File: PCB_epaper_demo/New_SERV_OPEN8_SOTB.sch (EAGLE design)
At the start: 71 parts, among them IC2 LT3082EST#PBF, IC3 RP105x, IC4 SN74AUP1G00DCKR, IC5 SN74AUP1G00DCKR, IC6 LM358AMX_NOPB, J1 TB006-508-02BE, J2 TB006-508-02BE, U1 SN74LVC1G32DBVR, U3 SN74AUP1G14DBVR, Y1 KC7050A48.0000C50D00

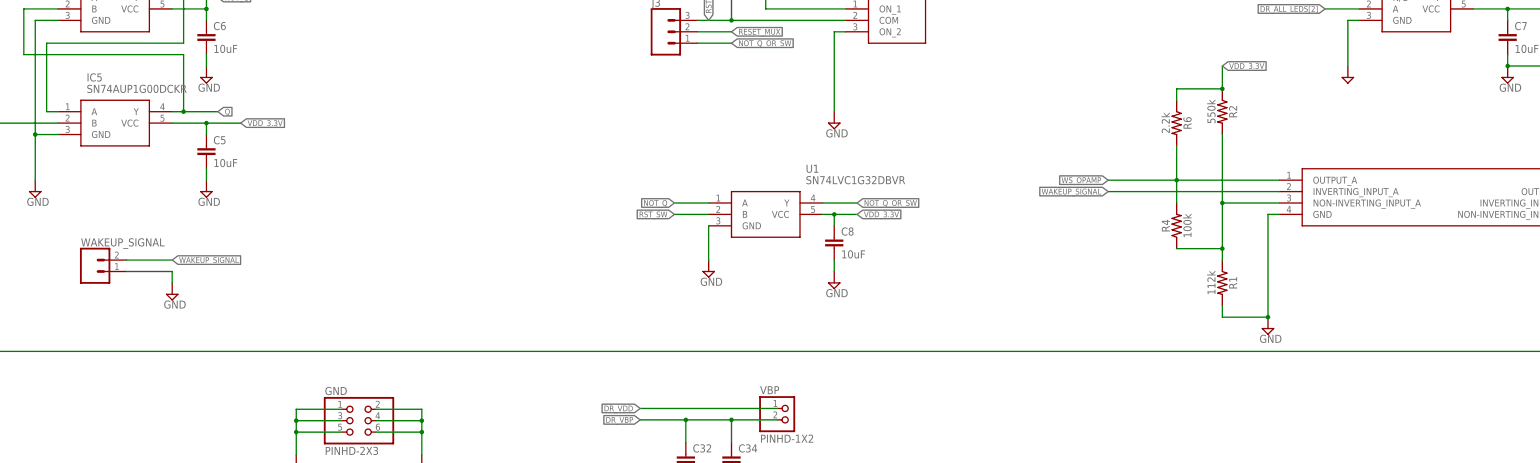
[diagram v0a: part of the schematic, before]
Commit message: add trimmer
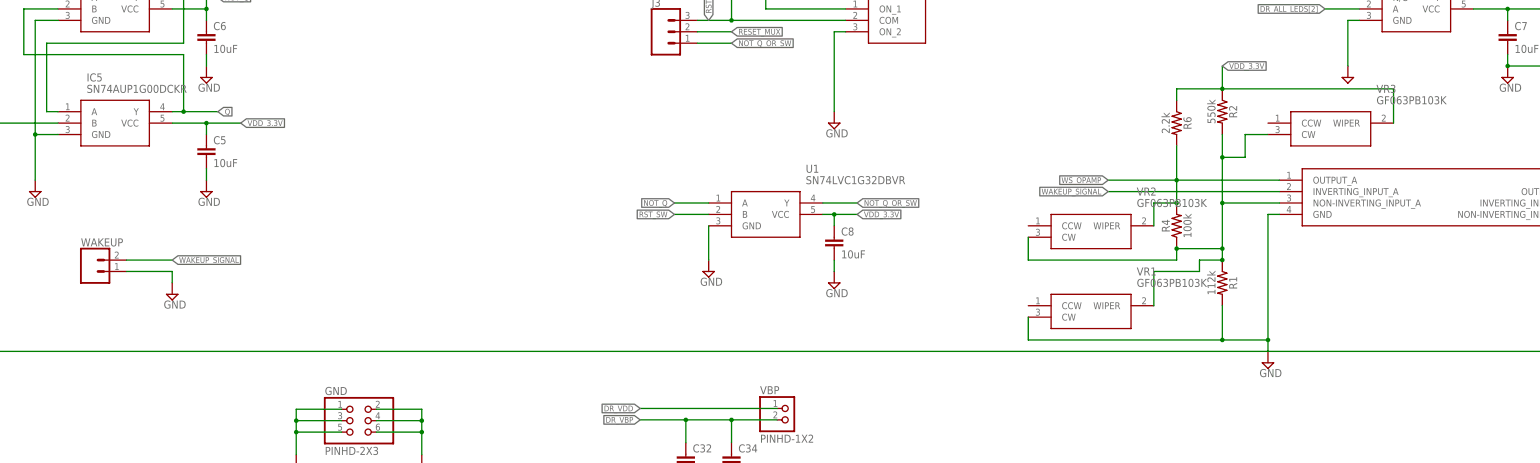
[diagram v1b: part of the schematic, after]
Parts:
- added VR1, VR2, VR3: GF063PB103K, SamacSys_Parts:GF063PB103K
- renumbered WAKEUP_SIGNAL to WAKEUP
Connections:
- net GND: now also VR1.CW
- net N$4: now also VR1.WIPER, VR2.CW, VR3.CW
- net VDD_3.3V: now also VR3.WIPER
- net WS_OPAMP: now also VR2.WIPER
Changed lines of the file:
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@@
 <part name="SUPPLY20" library="supply2" library_urn="urn:adsk.eagle:library:372" deviceset="GND" device=""/>
 <part name="LED" library="SparkFun-Connectors" library_urn="urn:adsk.eagle:library:513" deviceset="CONN_01" device="" package3d_urn="urn:adsk.eagle:package:38028/1"/>
-<part name="WAKEUP_SIGNAL" library="SparkFun-Connectors" library_urn="urn:adsk.eagle:library:513" deviceset="CONN_02" device="" package3d_urn="urn:adsk.eagle:package:38039/1"/>
+<part name="WAKEUP" library="SparkFun-Connectors" library_urn="urn:adsk.eagle:library:513" deviceset="CONN_02" device="" package3d_urn="urn:adsk.eagle:package:38039/1"/>
 <part name="SUPPLY21" library="supply2" library_urn="urn:adsk.eagle:library:372" deviceset="GND" device=""/>
 <part name="C9" library="SparkFun-Capacitors" library_urn="urn:adsk.eagle:library:510" deviceset="1.0UF" device="-0805-25V-(+80/-20%)" package3d_urn="urn:adsk.eagle:package:37429/1" value="0.1uF"/>
@@
 <part name="0.9V" library="Connector" library_urn="urn:adsk.eagle:library:16378166" deviceset="PINHD-1X3" device="" package3d_urn="urn:adsk.eagle:package:22458/2"/>
 <part name="R7" library="SparkFun-Resistors" library_urn="urn:adsk.eagle:library:532" deviceset="0.3OHM" device="-0805-1/8W-1%" package3d_urn="urn:adsk.eagle:package:39651/1" value="10k"/>
+<part name="VR1" library="SamacSys_Parts" deviceset="GF063PB103K" device=""/>
+<part name="VR2" library="SamacSys_Parts" deviceset="GF063PB103K" device=""/>
+<part name="VR3" library="SamacSys_Parts" deviceset="GF063PB103K" device=""/>
 </parts>
 <sheets>
@@
 <attribute name="NAME" x="154.94" y="106.172" size="1.778" layer="95" font="vector" rot="R180"/>
 </instance>
-<instance part="WAKEUP_SIGNAL" gate="G$1" x="-66.04" y="-76.2" smashed="yes">
+<instance part="WAKEUP" gate="G$1" x="-66.04" y="-76.2" smashed="yes">
 <attribute name="VALUE" x="-68.58" y="-81.026" size="1.778" layer="96" font="vector"/>
 <attribute name="NAME" x="-68.58" y="-70.612" size="1.778" layer="95" font="vector"/>
@@
 <attribute name="VALUE" x="265.43" y="-50.8" size="1.778" layer="96" align="center-left"/>
 </instance>
-<instance part="SUPPLY5" gate="GND" x="195.58" y="-88.9" smashed="yes">
-<attribute name="VALUE" x="193.675" y="-92.075" size="1.778" layer="96"/>
+<instance part="SUPPLY5" gate="GND" x="195.58" y="-96.52" smashed="yes">
+<attribute name="VALUE" x="193.675" y="-99.695" size="1.778" layer="96"/>
 </instance>
 <instance part="R1" gate="G$1" x="185.42" y="-78.74" smashed="yes" rot="R270">
@@
 <attribute name="NAME" x="77.724" y="-10.16" size="1.778" layer="95" font="vector" rot="R270" align="bottom-center"/>
 <attribute name="VALUE" x="74.676" y="-10.16" size="1.778" layer="96" font="vector" rot="R270" align="top-center"/>
+</instance>
+<instance part="VR1" gate="G$1" x="142.24" y="-83.82" smashed="yes">
+<attribute name="NAME" x="166.37" y="-76.2" size="1.778" layer="95" align="center-left"/>
+<attribute name="VALUE" x="166.37" y="-78.74" size="1.778" layer="96" align="center-left"/>
+</instance>
+<instance part="VR2" gate="G$1" x="142.24" y="-66.04" smashed="yes">
+<attribute name="NAME" x="166.37" y="-58.42" size="1.778" layer="95" align="center-left"/>
+<attribute name="VALUE" x="166.37" y="-60.96" size="1.778" layer="96" align="center-left"/>
+</instance>
+<instance part="VR3" gate="G$1" x="195.58" y="-43.18" smashed="yes">
+<attribute name="NAME" x="219.71" y="-35.56" size="1.778" layer="95" align="center-left"/>
+<attribute name="VALUE" x="219.71" y="-38.1" size="1.778" layer="96" align="center-left"/>
 </instance>
 </instances>
@@
 </segment>
 <segment>
-<pinref part="WAKEUP_SIGNAL" gate="G$1" pin="1"/>
+<pinref part="WAKEUP" gate="G$1" pin="1"/>
 <wire x1="-58.42" y1="-76.2" x2="-48.26" y2="-76.2" width="0.1524" layer="91"/>
 <pinref part="SUPPLY21" gate="GND" pin="GND"/>
@@
 <pinref part="IC6" gate="G$1" pin="GND"/>
 <wire x1="198.12" y1="-63.5" x2="195.58" y2="-63.5" width="0.1524" layer="91"/>
-<wire x1="195.58" y1="-63.5" x2="195.58" y2="-86.36" width="0.1524" layer="91"/>
+<wire x1="195.58" y1="-63.5" x2="195.58" y2="-91.44" width="0.1524" layer="91"/>
 <pinref part="SUPPLY5" gate="GND" pin="GND"/>
+<pinref part="VR1" gate="G$1" pin="CW"/>
+<wire x1="195.58" y1="-91.44" x2="195.58" y2="-93.98" width="0.1524" layer="91"/>
+<wire x1="142.24" y1="-86.36" x2="142.24" y2="-91.44" width="0.1524" layer="91"/>
 <pinref part="R1" gate="G$1" pin="2"/>
-<wire x1="185.42" y1="-83.82" x2="185.42" y2="-86.36" width="0.1524" layer="91"/>
-<wire x1="185.42" y1="-86.36" x2="195.58" y2="-86.36" width="0.1524" layer="91"/>
-<junction x="195.58" y="-86.36"/>
+<wire x1="142.24" y1="-91.44" x2="185.42" y2="-91.44" width="0.1524" layer="91"/>
+<wire x1="185.42" y1="-91.44" x2="185.42" y2="-83.82" width="0.1524" layer="91"/>
+<wire x1="185.42" y1="-91.44" x2="195.58" y2="-91.44" width="0.1524" layer="91"/>
+<junction x="185.42" y="-91.44"/>
+<junction x="195.58" y="-91.44"/>
 </segment>
 <segment>
@@
 <wire x1="175.26" y1="-35.56" x2="185.42" y2="-35.56" width="0.1524" layer="91"/>
 <junction x="185.42" y="-35.56"/>
+<wire x1="185.42" y1="-35.56" x2="223.52" y2="-35.56" width="0.1524" layer="91"/>
+<pinref part="VR3" gate="G$1" pin="WIPER"/>
+<wire x1="223.52" y1="-35.56" x2="223.52" y2="-43.18" width="0.1524" layer="91"/>
 </segment>
 <segment>
@@
 <net name="WAKEUP_SIGNAL" class="0">
 <segment>
-<pinref part="WAKEUP_SIGNAL" gate="G$1" pin="2"/>
+<pinref part="WAKEUP" gate="G$1" pin="2"/>
 <wire x1="-58.42" y1="-73.66" x2="-48.26" y2="-73.66" width="0.1524" layer="91"/>
 <label x="-48.26" y="-73.66" size="1.27" layer="95" xref="yes"/>
@@
 <wire x1="175.26" y1="-55.88" x2="175.26" y2="-48.26" width="0.1524" layer="91"/>
 <pinref part="R6" gate="G$1" pin="2"/>
+<pinref part="VR2" gate="G$1" pin="WIPER"/>
+<wire x1="170.18" y1="-66.04" x2="170.18" y2="-60.96" width="0.1524" layer="91"/>
+<wire x1="170.18" y1="-60.96" x2="175.26" y2="-60.96" width="0.1524" layer="91"/>
+<junction x="175.26" y="-60.96"/>
 </segment>
 </net>
@@
 <wire x1="185.42" y1="-60.96" x2="185.42" y2="-71.12" width="0.1524" layer="91"/>
 <wire x1="185.42" y1="-71.12" x2="185.42" y2="-73.66" width="0.1524" layer="91"/>
-<wire x1="185.42" y1="-60.96" x2="185.42" y2="-45.72" width="0.1524" layer="91"/>
+<wire x1="185.42" y1="-60.96" x2="185.42" y2="-50.8" width="0.1524" layer="91"/>
 <junction x="185.42" y="-60.96"/>
 <pinref part="R2" gate="G$1" pin="2"/>
 <pinref part="R4" gate="G$1" pin="1"/>
+<wire x1="185.42" y1="-50.8" x2="185.42" y2="-45.72" width="0.1524" layer="91"/>
 <wire x1="185.42" y1="-71.12" x2="175.26" y2="-71.12" width="0.1524" layer="91"/>
 <junction x="185.42" y="-71.12"/>
-</segment>
-</net>
+<pinref part="VR2" gate="G$1" pin="CW"/>
+<wire x1="142.24" y1="-68.58" x2="142.24" y2="-73.66" width="0.1524" layer="91"/>
+<wire x1="142.24" y1="-73.66" x2="175.26" y2="-73.66" width="0.1524" layer="91"/>
+<wire x1="175.26" y1="-73.66" x2="175.26" y2="-71.12" width="0.1524" layer="91"/>
+<junction x="175.26" y="-71.12"/>
+<pinref part="VR1" gate="G$1" pin="WIPER"/>
+<wire x1="170.18" y1="-83.82" x2="170.18" y2="-76.2" width="0.1524" layer="91"/>
+<wire x1="170.18" y1="-76.2" x2="180.34" y2="-76.2" width="0.1524" layer="91"/>
+<wire x1="180.34" y1="-76.2" x2="180.34" y2="-73.66" width="0.1524" layer="91"/>
+<wire x1="180.34" y1="-73.66" x2="185.42" y2="-73.66" width="0.1524" layer="91"/>
+<junction x="185.42" y="-73.66"/>
+<pinref part="VR3" gate="G$1" pin="CW"/>
+<wire x1="195.58" y1="-45.72" x2="190.5" y2="-45.72" width="0.1524" layer="91"/>
+<wire x1="190.5" y1="-45.72" x2="190.5" y2="-50.8" width="0.1524" layer="91"/>
+<wire x1="190.5" y1="-50.8" x2="185.42" y2="-50.8" width="0.1524" layer="91"/>
+<junction x="185.42" y="-50.8"/>
+</segment>
+</net>
